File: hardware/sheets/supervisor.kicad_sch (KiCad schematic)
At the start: 21 parts, among them J1 QSPI_FLASH, J2 USB_HOST, J3 POST_HEX, J4 CONSOLE, J5 SWD, U1 RP2040, Y1 12MHz

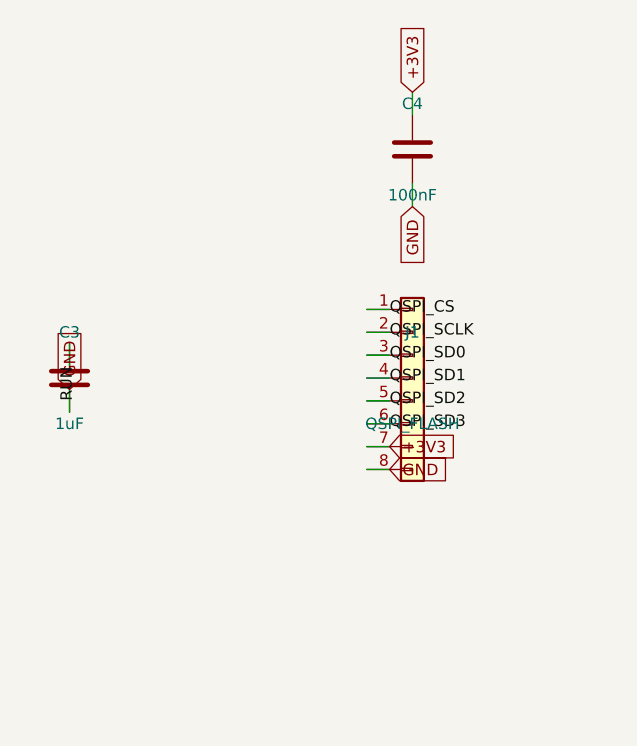
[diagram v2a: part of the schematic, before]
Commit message: JLCPCB sourcing pass: verify pinouts, LCSC part numbers, SMD build
Custom-symbol verification (open-questions Q5 resolved):
- MAX3241 symbol was wrong on nearly every pin and used MAX3243-style
  control names; regenerated to the real SSOP-28 pinout (SHDN#/EN#/
  R1OUTB/R2OUTB) and com_port rewired -- EN# must be GROUNDED (the old
  ~FORCEON-high would have disabled the receivers on real silicon)
- DS12C887 symbol wrong on 4 pins (DS=17, RESET#=18, IRQ#=19, SQW=23)

Sourcing (every part checked against the JLC DB; ~45 line items):
- New tools/parts.py maps (lib_id, value) -> LCSC; build.py applies it as
  an 'LCSC Part Num' property on every component (384 across the project)
- Sheets stay generic; stock-forced substitutions bound in the map:
  '374->'574 (parallel rewired), '163->'161, '157->HC157 (+HCT-buffered
  3.3V selects, I0/I1 swapped), '02->HC02, TCM809->MCP809, 2N3904->MMBT3904
- bus_mcu address counters moved to the 3.3V domain (HC161 on 3V3_BUS,
  loaded from MCU-side MD0-7; HCT244s read the 3.3V outputs at TTL Vih)
- 14.318 XOs are 3.3V-only parts: powered from 3V3, squared up via spare
  HCT gates (cpu_core U13, card_isatest U19)
- COM baud reference is now a 1.8432MHz crystal on the 16C550's XIN/XOUT
  (3.3V-only oscillators vs a 5V-only soft card)
- Supervisor QSPI header replaced with a real W25Q128JVSIQ
- Socket policy (fab installs sockets): V20 DIP-40, SRAM DIP-32 (no 5V
  512Kx8 SRAM at JLC at all), DS12C887 DIP-24, female headers for modules

Docs: CLAUDE.md fabrication-constraints section (SMD, 100x100mm, generic-
symbols rule, voltage-domain rule); README + hardware/README fab notes;
notes/jlcpcb-sourcing.md (decisions, thin-stock flags, not-at-JLC list);
stale questions-sidecar.md collapsed to its supersession record.

Rebuilt motherboard + cards: structural ERC 0, byte-identical rebuilds.

Co-Authored-By: Claude Fable 5 <noreply@anthropic.com>
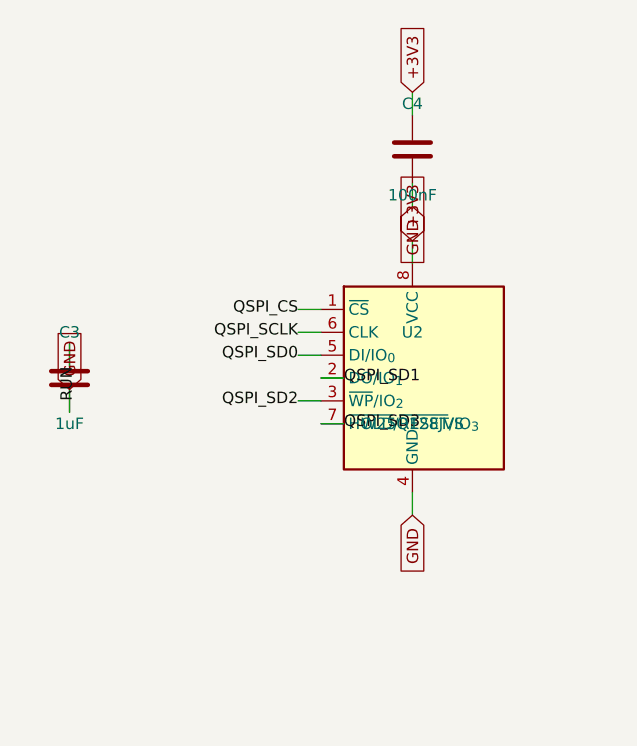
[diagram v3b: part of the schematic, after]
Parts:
- C1, C2: LCSC Part Num (none) -> C1644
- C10, C11, C12, C4, C5, C7, C8, C9: LCSC Part Num (none) -> C14663
- C3: LCSC Part Num (none) -> C15849
- C6: LCSC Part Num (none) -> C15850
- F1: LCSC Part Num (none) -> C46641014
- J2: LCSC Part Num (none) -> C456015
- J3, J4, J5: LCSC Part Num (none) -> C2337
- R1: LCSC Part Num (none) -> C25804
- U1: LCSC Part Num (none) -> C2040
- U2: renamed from J1; value QSPI_FLASH -> W25Q128JVS; symbol Connector_Generic:Conn_01x08 -> Memory_Flash:W25Q128JVS; LCSC Part Num (none) -> C97521
- Y1: LCSC Part Num (none) -> C9002
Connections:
- net +3V3: now also U2.8 (VCC); no longer U2.7 (Pin_7)
- net GND: now also U2.4 (GND); no longer U2.8 (Pin_8)
- net QSPI_SCLK: now also U2.6 (CLK); no longer U2.2 (Pin_2)
- net QSPI_SD0: now also U2.5 (DI/IO_{0}); no longer U2.3 (Pin_3)
- net QSPI_SD1: now also U2.2 (DO/IO_{1}); no longer U2.4 (Pin_4)
- net QSPI_SD2: now also U2.3 (~{WP}/IO_{2}); no longer U2.5 (Pin_5)
- net QSPI_SD3: now also U2.7 (~{HOLD}/~{RESET}/IO_{3}); no longer U2.6 (Pin_6)
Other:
- moved on the sheet: U2

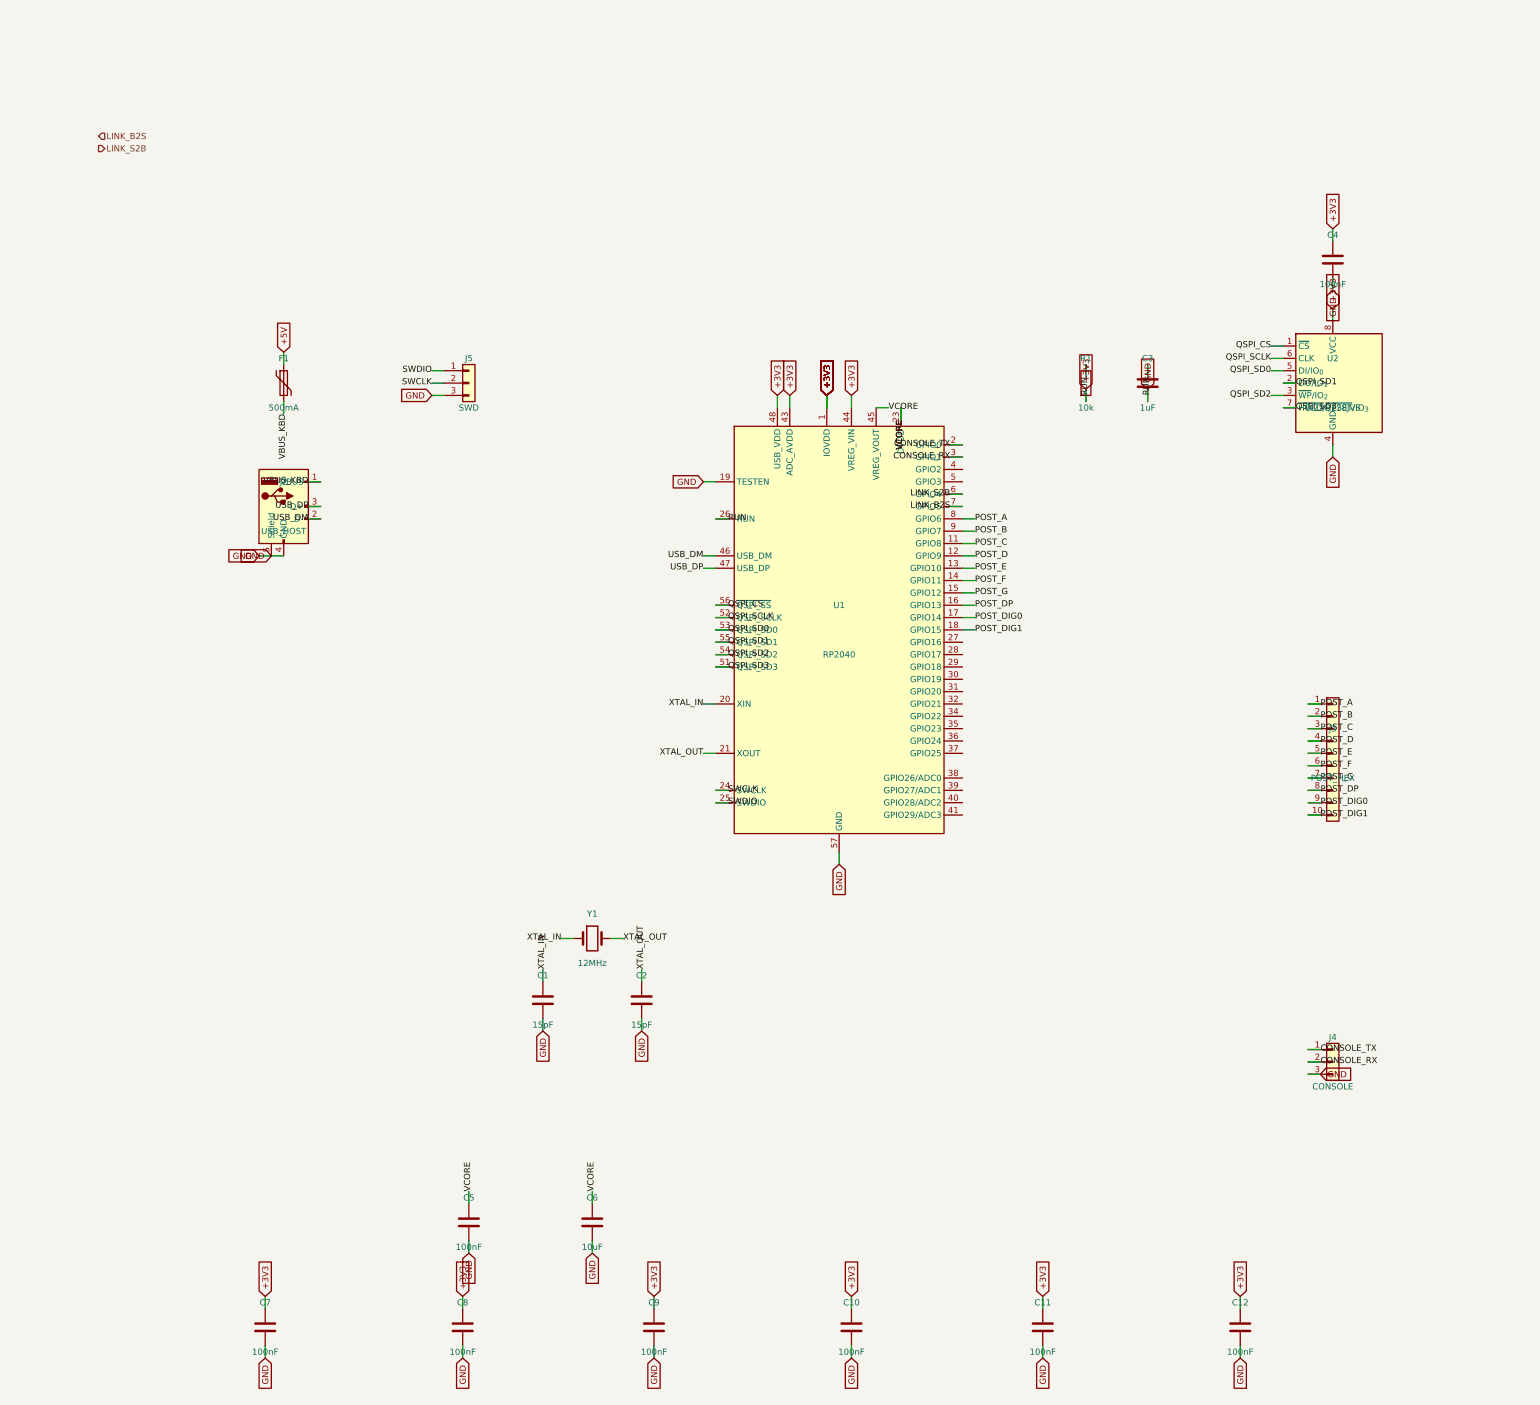
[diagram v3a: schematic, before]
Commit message: Design review 2026-07-11: rail protection, decoupling, wiring fixes
Protection:
- Sidecar +5V now feeds through a 2A polyfuse into +5V_ISA with an
  SMBJ5.0A clamp + 22uF bulk (a faulted ISA card trips its own fuse
  instead of dropping the board; back-fed voltage is clamped).
- USB-C VBUS enters through a 3A polyfuse with an SMBJ5.0A on +5V
  (backstop for the CFG1 9-20V failure mode). CH224K gains a 1uF VDD
  cap; its PG routes to Supervisor GPIO16 as PD_PG. Buck output
  doubled to 2x22uF, 10uF at VIN, extra rail bulk.
- Supervisor USB-A host port: 27R series termination (RP2040
  requirement), USBLC6-2SC6 ESD array, 100uF VBUS bulk.
- Video: HDMI +5V fused (500mA), HPD sensed on GPIO41, 100R series on
  VGA sync. TMDS ESD array deferred to layout (no symbol).
- card_isatest: V5RAW bulk, Q1 gate soft-start cap, TVS on DUT rail.

Wiring fixes:
- SPKR had no driver anywhere (netlist: 1 node). Bus MCU GPIO22
  reassigned from the diagnostics-only bus-CLK sense to SPKR; bus_mcu
  drops CLK from its interface. Doc 5.2 updated.
- bus_mcu C8 decoupled +3V3, a rail that sheet never uses -> 3V3_BUS.
- Storage IRQ5 was push-pull (permanently driven when idle) -> 2N7002
  + gated '125 tri-state, same convention as the LPT IRQ7 stage.
- MAX3241 pump caps resized to the 5V datasheet values (47nF/330nF).
- LPT DB25 status inputs get 4.7k pull-ups (floated with no printer).
- Audio line-out gets a 100R series isolator before the jack.

Best practices:
- Decoupling to ~1x100nF per IC on every sheet + bulk per board
  (cpu_core 7->16 incl. the naked 3.3V oscillator, storage 4->11,
  parallel 6->13, rtc/com/video/bus_mcu/card_isatest similar).
- All floating spare CMOS inputs tied ('00/'74/'157/'02/'04/'125
  sections across cpu_core, bus_mcu, rtc, storage, card_isatest).

Sourcing: new parts mapped in parts.py with JLC-verified LCSC numbers;
Power_Protection lib registered in the tools; TPS563200 stock alert
(4 pcs left at JLC) flagged in parts.py + jlcpcb-sourcing.md. All
decisi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
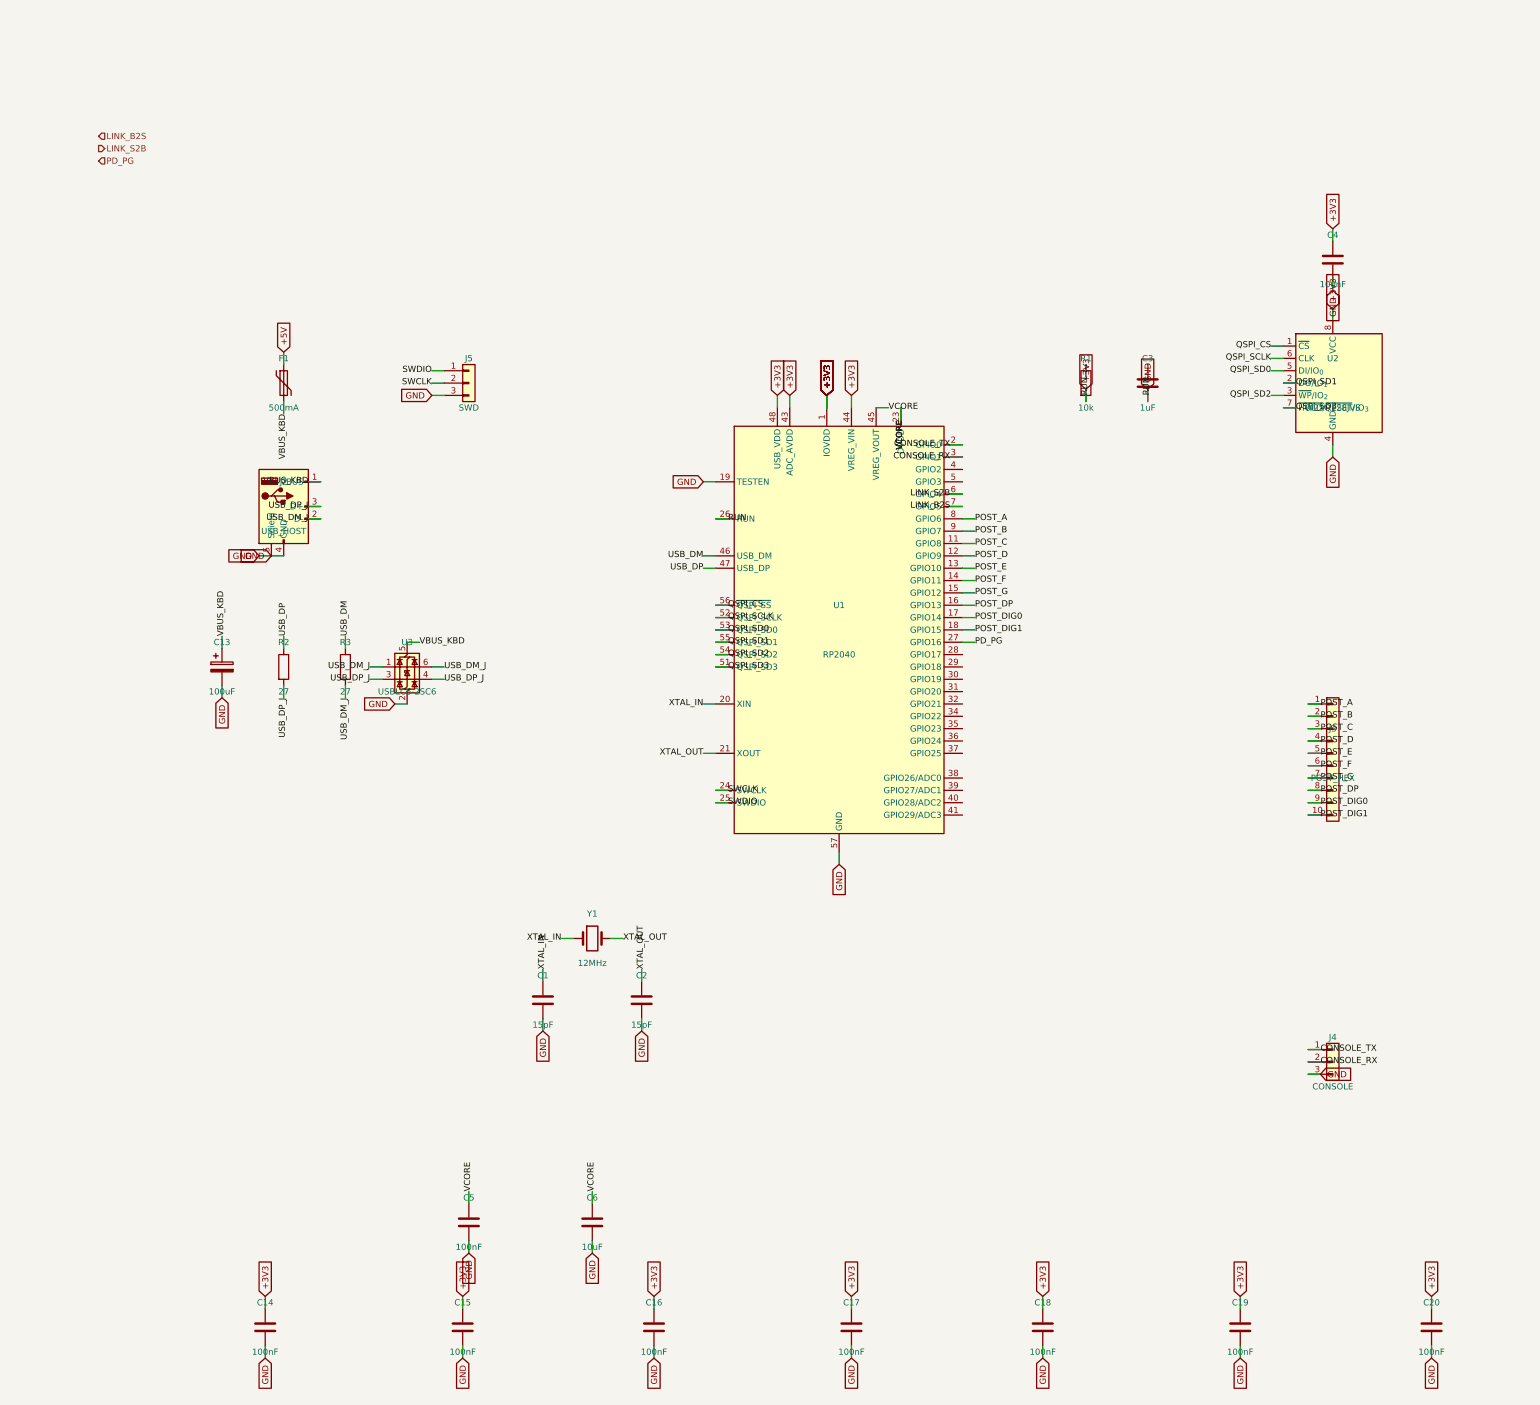
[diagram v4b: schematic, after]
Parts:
- removed C10, C11, C12, C7, C8, C9: 100nF, symbol Device:C
- removed J2: USB_HOST, symbol Connector:USB_A
- added C13: 100uF, symbol Device:C_Polarized
- added C14, C15, C16, C17, C18, C19, C20: 100nF, symbol Device:C
- added F1: 500mA, symbol Device:Polyfuse
- added R2, R3: 27, symbol Device:R
- added U3: USBLC6-2SC6, symbol Power_Protection:USBLC6-2SC6
- J2: renamed from F1; value 500mA -> USB_HOST; symbol Device:Polyfuse -> Connector:USB_A; LCSC Part Num C46641014 -> C456015
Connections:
- net +3V3: now also C14.1, C15.1, C16.1, C17.1, C18.1, C19.1, C20.1
- net +5V: now also F1.1; no longer J2.1
- net GND: now also J2.4 (GND), J2.5 (Shield), C13.2, C14.2, C15.2, C16.2, C17.2, C18.2, C19.2, C20.2, U3.2 (GND)
- net USB_DM: now also R3.1
- net USB_DP: now also R2.1
- net VBUS_KBD: now also J2.1 (VBUS), C13.1, F1.2, U3.5 (VBUS); no longer J2.2
- net PD_PG: now reaches U1.27 (GPIO16)
- new net USB_DM_J: J2.2 (D-), R3.2, U3.1 (I/O1), U3.6 (I/O1)
- new net USB_DP_J: J2.3 (D+), R2.2, U3.3 (I/O2), U3.4 (I/O2)

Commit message: PicoGUS on-board: chip-down transcription + shared RP2040 programming port
New picogus sheet (bank 13): a pin-faithful copy of polpo's PicoGUS 2.0
chip-down design (CERN-OHL-P, picogus/hw-chipdown sources) running STOCK
firmware -- the RP2040 GPIO map was extracted from the reference netlist
and our netlist matches it 30-for-30. Copied verbatim: the ADS-muxed
shared AD0-AD7 bus through SN74CB3T FET switches, the ~BUSOE power-up
latch (bus switches off until firmware first toggles ADS), AEN.DACK
IOR/IOW masking, open-drain IOCHRDY, APS6404L-3SQR sample PSRAM, PCM5102A
I2S DAC, IRQ/DMA jumper block (DMA must be jumpered to ch1, the only
MCU-serviced channel; IRQ5 is free since storage moved to IRQ14), AMS1117
local 3V3 island with ferrite-split AVDD/AGND, GPIO29-grounded board
detect, BOOTSEL + LED.

Deviations from the reference (user decisions, logged in
questions-picogus.md): no USB-A gameport (Supervisor owns HID; 0x201
unused), no wavetable header and no MIDI-out jack (build simplification --
the M62429 volume chip and passive mix node went with them; the firmware's
RV_CLK/RV_DATA/MIDI_TX pins are documented no-connects), no local audio
jack (RC-filtered DAC output leaves as PG_L/PG_R into the audio summer ->
the board's one line-out), no local programming USB.

Supervisor: crystal corrected to 30pF + 1k XOUT (same 12MHz part both
RP2040s -- fewer line items), BOOTSEL button added, and J6/SW2 form ONE
USB-C programming port for both bare RP2040s (DPDT slide: A = Supervisor,
C = PicoGUS; KiCad's SW_Slide_DPDT commons are the middle B pins -- the
first draft wired C as common and was corrected). J6 VBUS is unconnected:
the board must be powered to flash, so no back-power path exists.
PGUS_USB_DP/DM are a documented soft-card isolation exception (mxbus
PRIV_PROG); lifting the card means deleting them and fitting a connector.

Audio sheet: J1 line-in stub replaced by PG_L/PG_R interface pins.

Toolchain: six new flat symbols (CB3T3257/CB3T3245/74LVC2G06/PCM5102A/
M62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
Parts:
- added J6: USB_PROG, symbol Connector:USB_C_Receptacle
- added R4, R5: 1k, symbol Device:R
- added R6, R7: 5.1k, symbol Device:R
- added SW1: BOOTSEL, symbol Switch:SW_Push
- added SW2: PROG SEL, symbol Switch:SW_Slide_DPDT
- C1, C2: value 15pF -> 30pF; LCSC Part Num C1644 -> C1658
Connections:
- net GND: now also J6.A1 (GND), J6.A12 (GND), J6.B1 (GND), J6.B12 (GND), J6.S1 (SHIELD), R6.2, R7.2, SW1.2
- net QSPI_CS: now also R5.1
- net USB_DM_J: now also SW2.4 (A)
- net USB_DP_J: now also SW2.1 (A)
- net XTAL_OUT: now also R4.2; no longer C2.1, U1.21 (XOUT), Y1.2
- new net: J6.A4 (VBUS), J6.A9 (VBUS), J6.B4 (VBUS), J6.B9 (VBUS)
- new net PGUS_USB_DM: SW2.6 (C)
- new net PGUS_USB_DP: SW2.3 (C)
- new net PROG_CC1: J6.A5 (CC1), R6.1
- new net PROG_CC2: J6.B5 (CC2), R7.1
- new net PROG_DM: J6.A7 (D-), J6.B7 (D-), SW2.5 (B)
- new net PROG_DP: J6.A6 (D+), J6.B6 (D+), SW2.2 (B)
- new net XOUT_R: C2.1, R4.1, U1.21 (XOUT), Y1.2
- new net ~{USB_BOOT}: R5.2, SW1.1
- no-connect marks 0 -> 14
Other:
- title: Supervisor MCU (RP2040) -- USB host, setup UI, config/flash, POST, console -> Supervisor MCU (RP2040) -- USB host, setup UI, config/flash, POST, console, shared prog port
